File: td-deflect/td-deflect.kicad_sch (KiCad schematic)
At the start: 77 parts, among them J10 Conn_01x02_Male, J11 Conn_01x02_Male, J12 Conn_01x06_Male, J3 Conn_01x02_Male, Q1 BSC082N10LSG, Q10 IPD50R380CE, Q11 IPD50R380CE, Q2 C2M0045170D, Q3 BSC082N10LSG, Q4 BCP56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

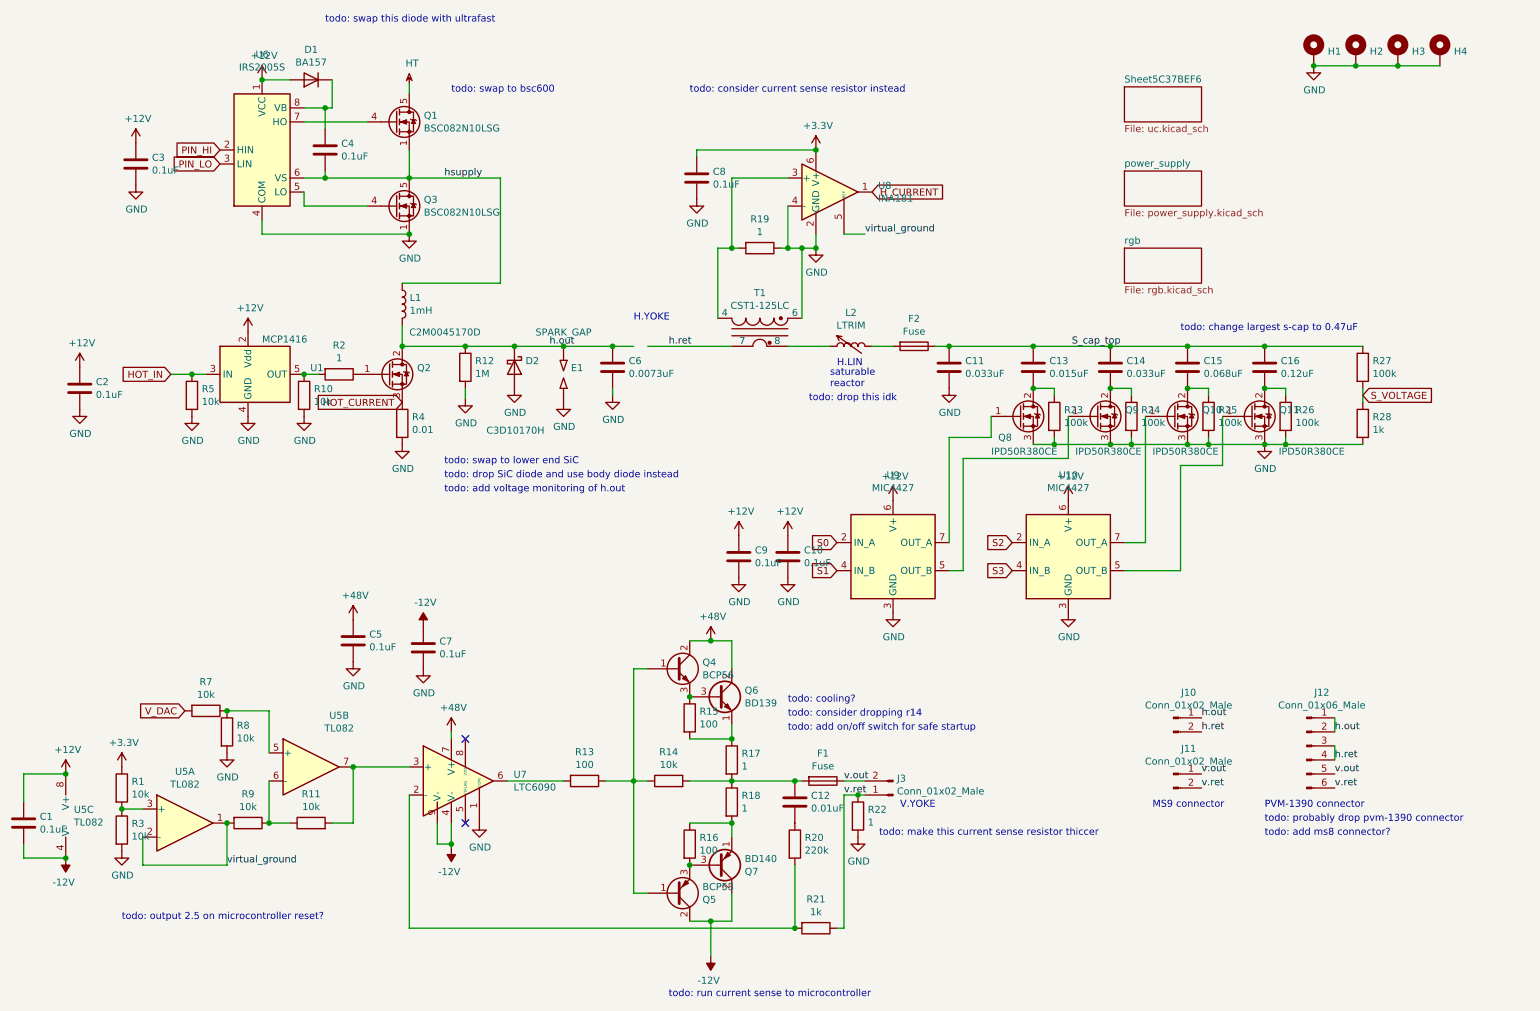
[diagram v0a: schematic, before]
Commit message: update some transistors, remove current sense amp
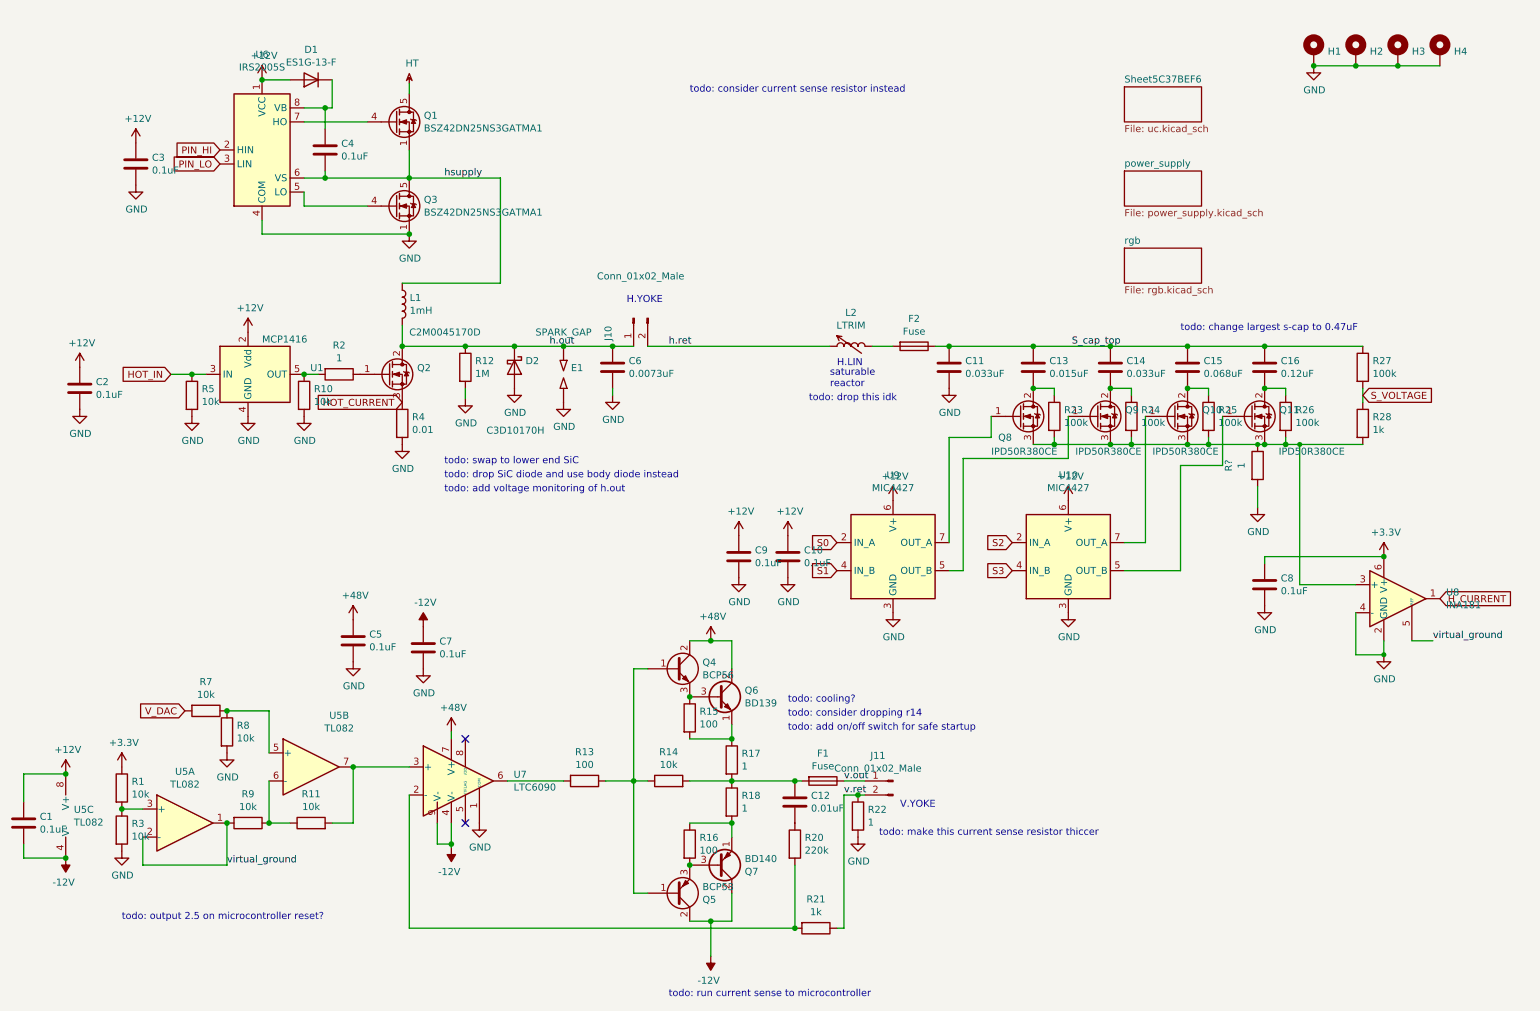
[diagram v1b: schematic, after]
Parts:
- removed J12: Conn_01x06_Male, td-deflect:sony_monitor_yoke, symbol Connector:Conn_01x06_Male
- removed J3: Conn_01x02_Male, Connector_Phoenix_MSTB:PhoenixContact_MSTBVA_2,5_2-G_1x02_P5.00mm_Vertical, symbol Connector:Conn_01x02_Male
- removed R19: 1, Resistor_SMD:R_0805_2012Metric_Pad1.15x1.40mm_HandSolder, symbol Device:R
- removed T1: CST1-125LC, Transformer_SMD:Transformer_Coilcraft_CST1, symbol Transformer:CST1
- added R?: 1, Resistor_SMD:R_0805_2012Metric_Pad1.15x1.40mm_HandSolder, symbol Device:R
- D1: value BA157 -> ES1G-13-F; footprint Diode_THT:D_DO-41_SOD81_P10.16mm_Horizontal -> Diode_SMD:D_SMA; Digikey BA157-E3/54GICT-ND -> ES1G-FDICT-ND
- Q1, Q3: value BSC082N10LSG -> BSZ42DN25NS3GATMA1; Digikey BSC082N10LSGATMA1CT-ND -> BSZ42DN25NS3GATMA1CT-ND
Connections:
- net GND: now also R?.2; no longer Q10.3 (S), Q11.3 (S), Q8.3 (S), Q9.3 (S), R23.2, R24.2, R25.2, R26.2, R28.2
- net h.ret: now also L2.1
- net at U8.3 (+): now also Q10.3 (S), Q11.3 (S), Q8.3 (S), Q9.3 (S), R23.2, R24.2, R25.2, R26.2, R28.2, R?.1
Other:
- note removed: "MS9 connector"
- note removed: "PVM-1390 connector"
- note removed: "todo: add ms8 connector?"
- note removed: "todo: probably drop pvm-1390 connector"
- note removed: "todo: swap this diode with ultrafast"
- note removed: "todo: swap to bsc600"
- moved on the sheet: C8, J10, J11, U8

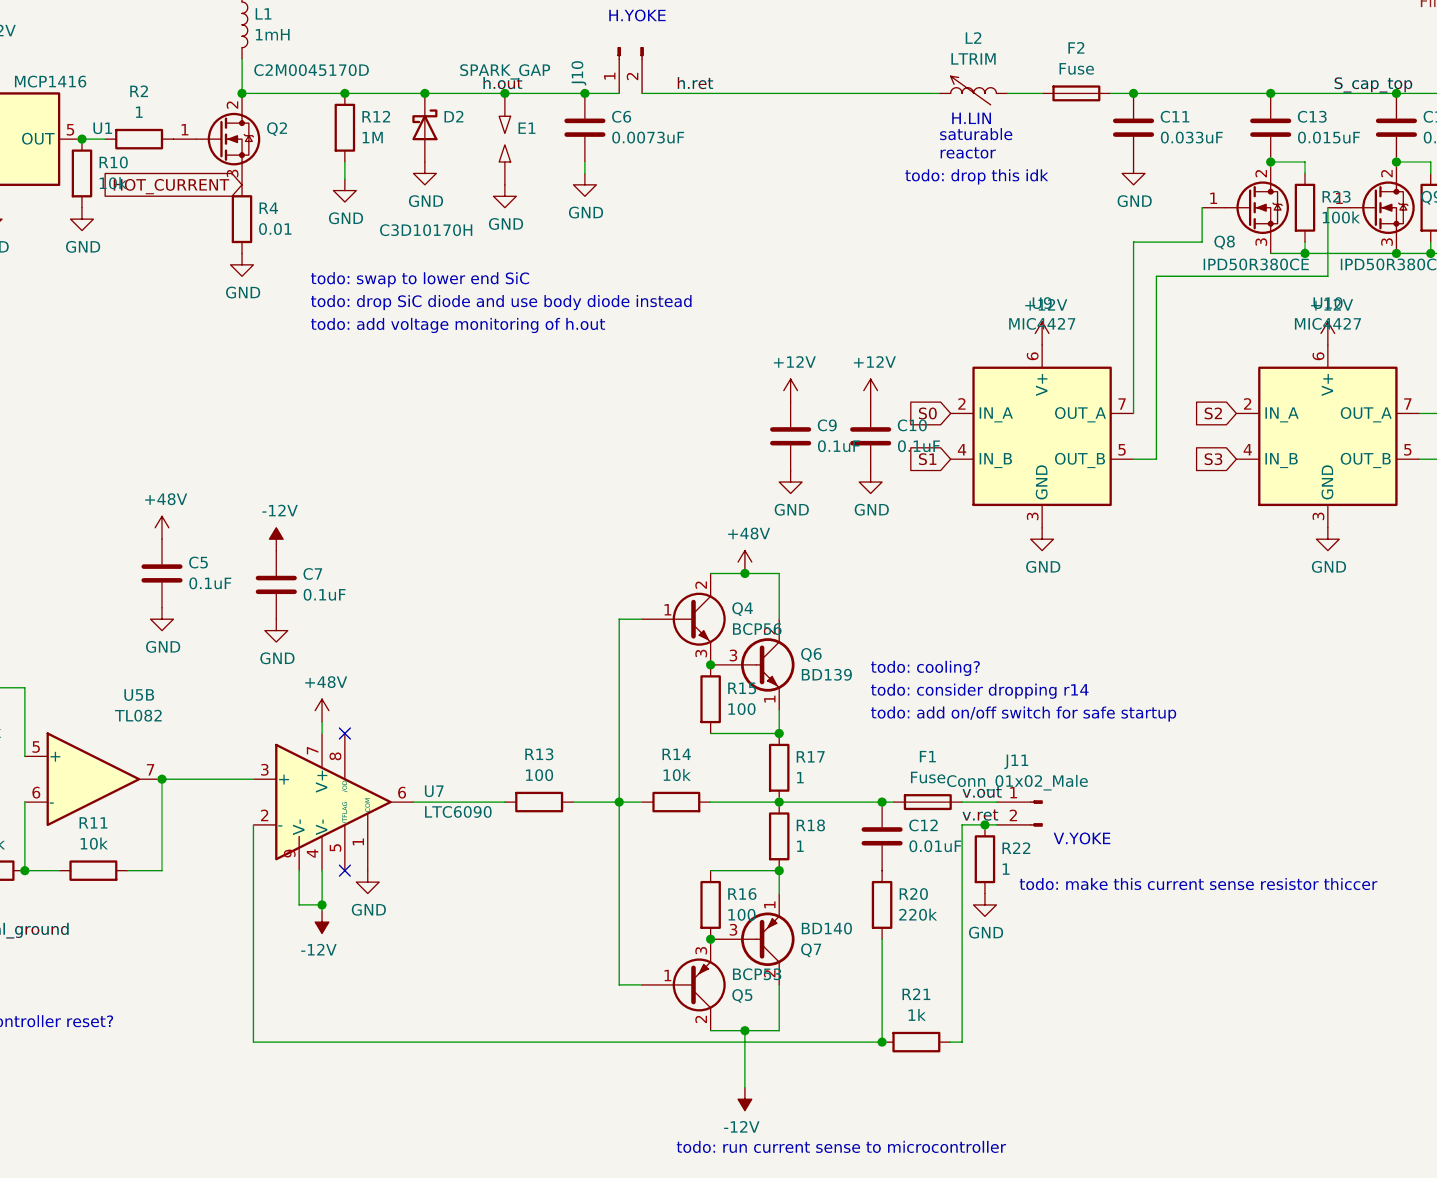
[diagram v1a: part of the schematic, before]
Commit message: new vertical amp
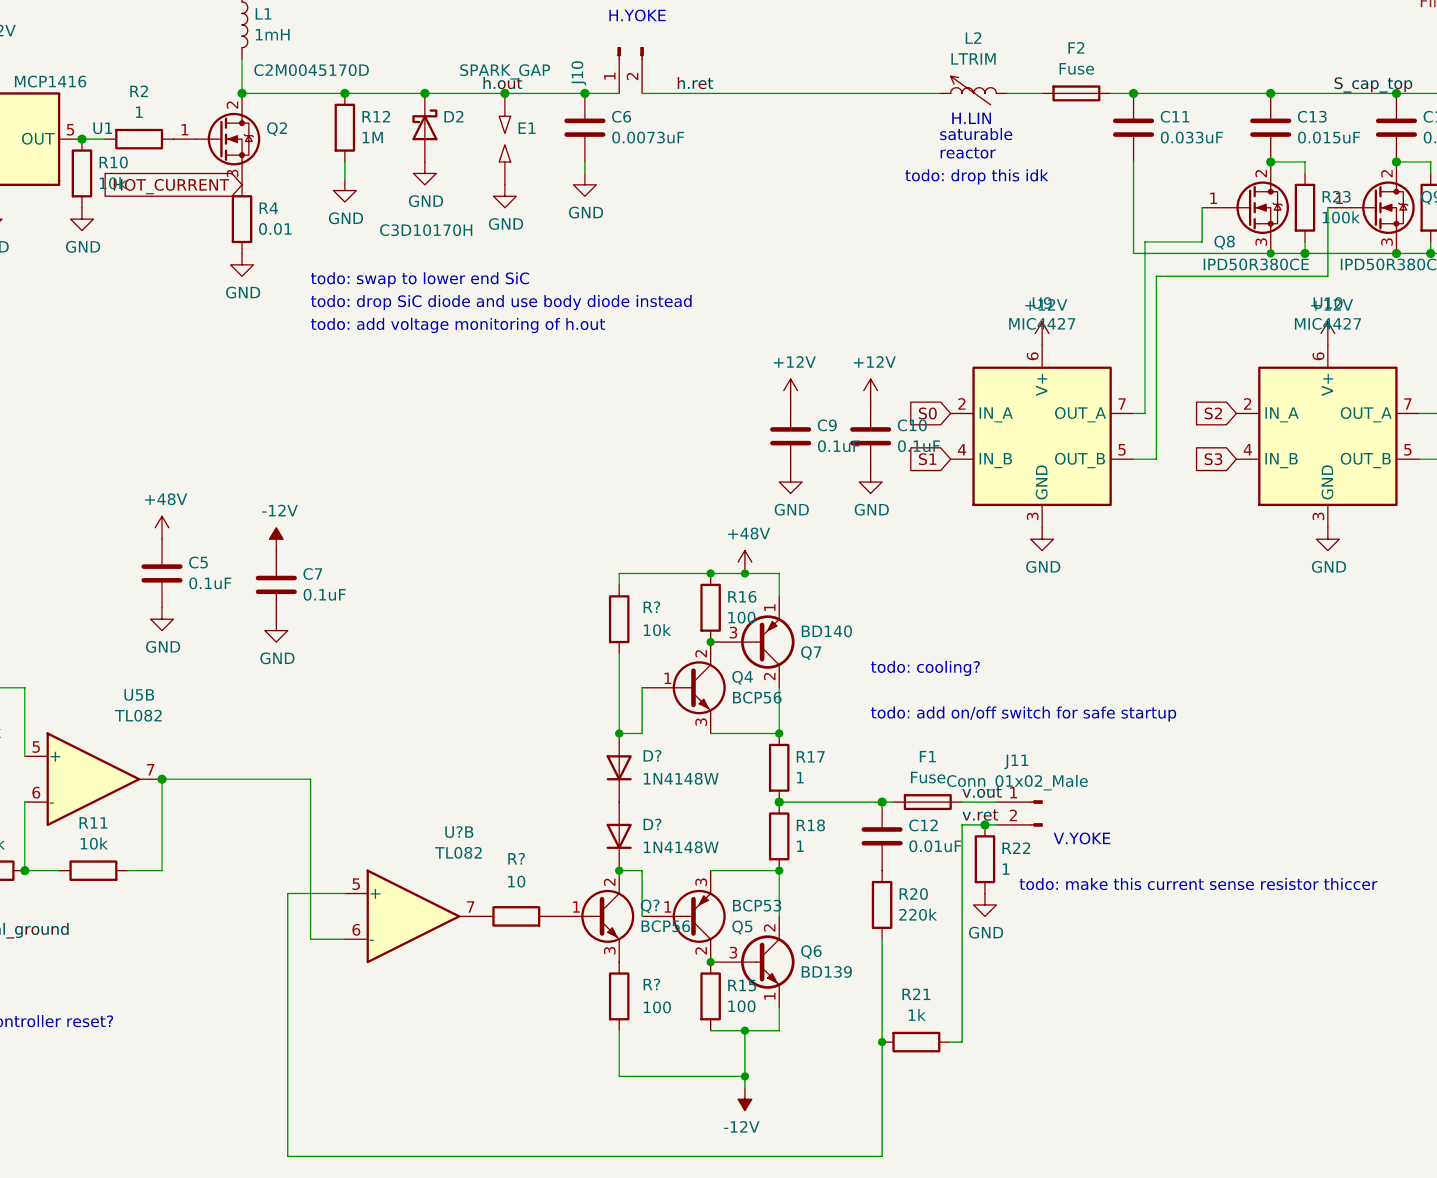
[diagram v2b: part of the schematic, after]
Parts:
- removed R13: 100, Resistor_SMD:R_0805_2012Metric_Pad1.15x1.40mm_HandSolder, symbol Device:R
- removed R14: 10k, Resistor_SMD:R_0805_2012Metric_Pad1.15x1.40mm_HandSolder, symbol Device:R
- removed U7: LTC6090, Package_SO:SOIC-8-1EP_3.9x4.9mm_P1.27mm_EP2.29x3mm, symbol td-deflect:LTC6090
- added D? (x2): 1N4148W, Diode_SMD:D_SOD-123, symbol Diode:1N4148W
- added Q?: BCP56, Package_TO_SOT_SMD:SOT-223-3_TabPin2, symbol Transistor_BJT:BCP56
- added R?: 10k, Resistor_SMD:R_1210_3225Metric, symbol Device:R
- added R?: 10, symbol Device:R
- added R?: 100, symbol Device:R
- added U?: TL082, Package_SO:SOIC-8_3.9x4.9mm_P1.27mm, symbol Amplifier_Operational:TL082
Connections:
- net +48V: now also Q7.1 (E), R16.1, R?.1; no longer Q4.2 (C), Q4.4 (C), Q6.2 (C)
- net -12V: now also Q6.1 (E), R15.2, R?.2; no longer Q5.2 (C), Q5.4 (C), Q7.2 (C)
- net GND: no longer C11.2
- net at Q10.3 (S), Q11.3 (S), Q8.3 (S)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: now also C11.2
- net at Q7.3 (B), R16.2: now also Q4.2 (C), Q4.4 (C); no longer Q5.3 (E)
- net at Q6.3 (B), R15.1: now also Q5.2 (C), Q5.4 (C); no longer Q4.3 (E)
- net at Q5.1 (B): now also D?.1 (K), Q?.2 (C), Q?.4 (C); no longer Q4.1 (B)
- net at R20.2, R21.2: now also U?.5 (+)
- net at R11.2, U5.7: now also U?.6 (-)
- new net: Q4.3 (E), Q7.2 (C), R17.1
- new net: Q5.3 (E), Q6.2 (C), R18.2
- new net: D?.2 (A), Q4.1 (B), R?.2
- new net: R?.1, U?.7
- new net: Q?.1 (B), R?.2
- new net: Q?.3 (E), R?.1
- new net: D?.1 (K), D?.2 (A)
- no-connect marks 2 -> 0
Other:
- note removed: "todo: consider dropping r14"
- note removed: "todo: run current sense to microcontroller"
- moved on the sheet: Q4, Q5, Q6, Q7, R15, R16

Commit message: update vertical
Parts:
- added C?: 10uF 100V, symbol Device:C
- added D? (x2): 1N4148W, Diode_SMD:D_SOD-123, symbol Diode:1N4148W
- R22: footprint Resistor_SMD:R_0805_2012Metric_Pad1.15x1.40mm_HandSolder -> Resistor_SMD:R_1210_3225Metric; Digikey 311-1.00CRCT-ND -> (none)
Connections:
- net +48V: now also D?.1 (K), D?.2 (A); no longer R16.1, R?.1
- net at Q4.3 (E), Q7.2 (C), R17.1: now also D?.2 (A)
- net at C12.1, F1.2, R17.2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: now also C?.2
- new net: C?.1, D?.1 (K), R16.1, R?.1
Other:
- note removed: "todo: make this current sense resistor thiccer"
- moved on the sheet: C10, C9

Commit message: switch to newer sic mosfet
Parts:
- Q2: value C2M0045170D -> G3R450MT17D; Digikey C2M0045170D-ND -> 1242-G3R450MT17D-ND
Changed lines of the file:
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@@
       (effects (font (size 1.27 1.27)) (justify left))
     )
-    (property "Value" "C2M0045170D" (id 1) (at 87.63 73.66 0)
+    (property "Value" "G3R450MT17D" (id 1) (at 87.63 73.66 0)
       (effects (font (size 1.27 1.27)) (justify left))
     )
@@
       (effects (font (size 1.27 1.27) italic) hide)
     )
-    (property "Datasheet" "https://www.wolfspeed.com/media/downloads/960/C2M0045170D.000.pdf" (id 3) (at 83.82 81.28 0)
+    (property "Datasheet" "http://www.genesicsemi.com/sic-mosfet/G3R450MT17D/G3R450MT17D.pdf" (id 3) (at 83.82 81.28 0)
       (effects (font (size 1.27 1.27)) (justify left) hide)
     )
-    (property "Digikey" "C2M0045170D-ND" (id 4) (at 83.82 81.28 0)
+    (property "Digikey" "1242-G3R450MT17D-ND" (id 4) (at 83.82 81.28 0)
       (effects (font (size 1.27 1.27)) hide)
     )
@@
     )
     (path "/00000000-0000-0000-0000-00005c36718e"
-      (reference "Q2") (unit 1) (value "C2M0045170D") (footprint "Package_TO_SOT_THT:TO-247-3_Vertical")
+      (reference "Q2") (unit 1) (value "G3R450MT17D") (footprint "Package_TO_SOT_THT:TO-247-3_Vertical")
     )
     (path "/00000000-0000-0000-0000-00005dbc9c3e"
